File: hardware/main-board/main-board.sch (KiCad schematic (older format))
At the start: 0 parts

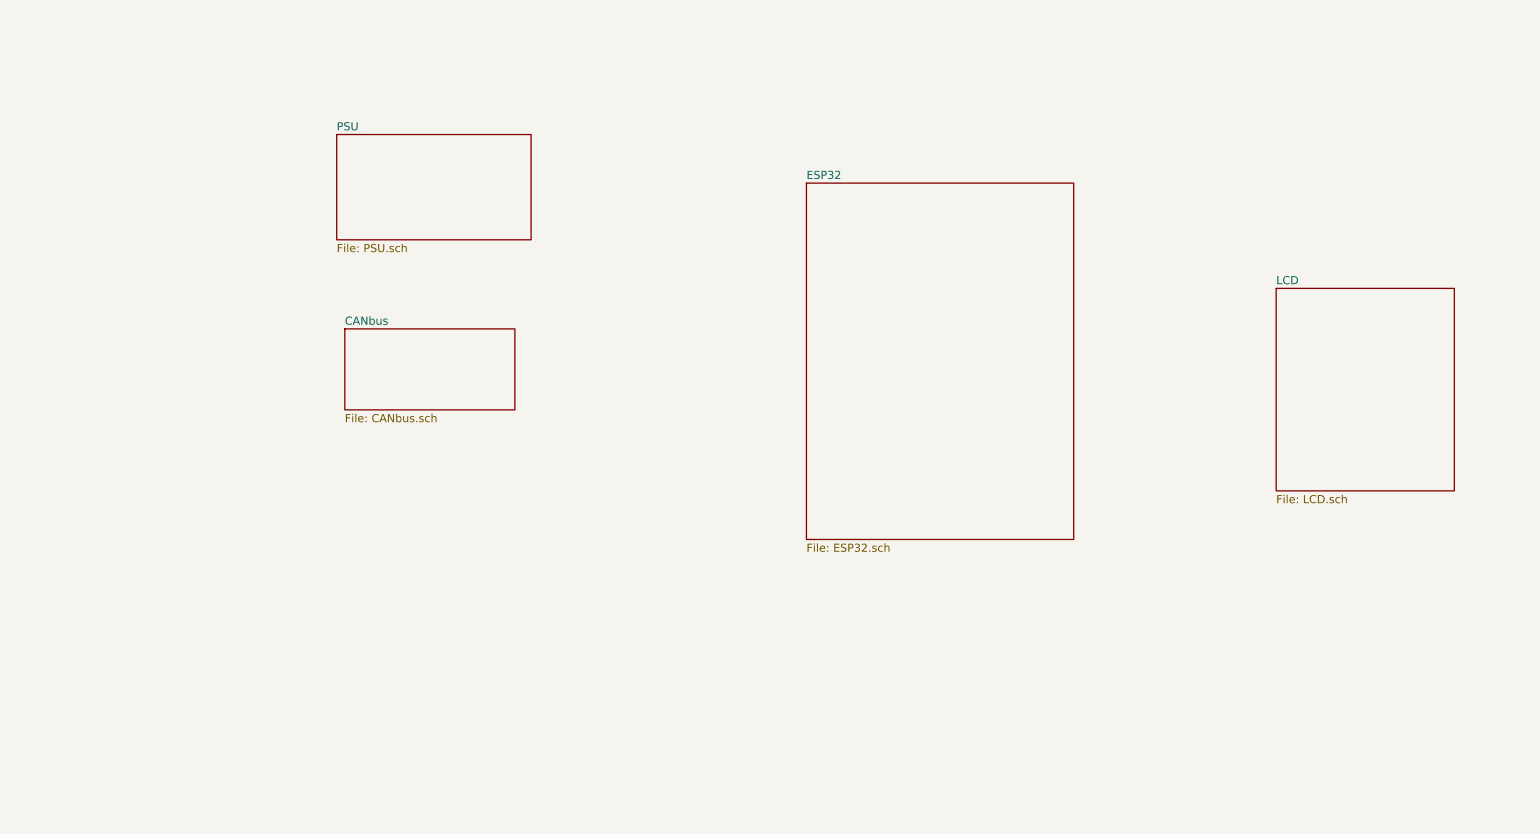
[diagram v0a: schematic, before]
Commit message: Sch mostly done, drew a few custom footprints, placement mostly done.
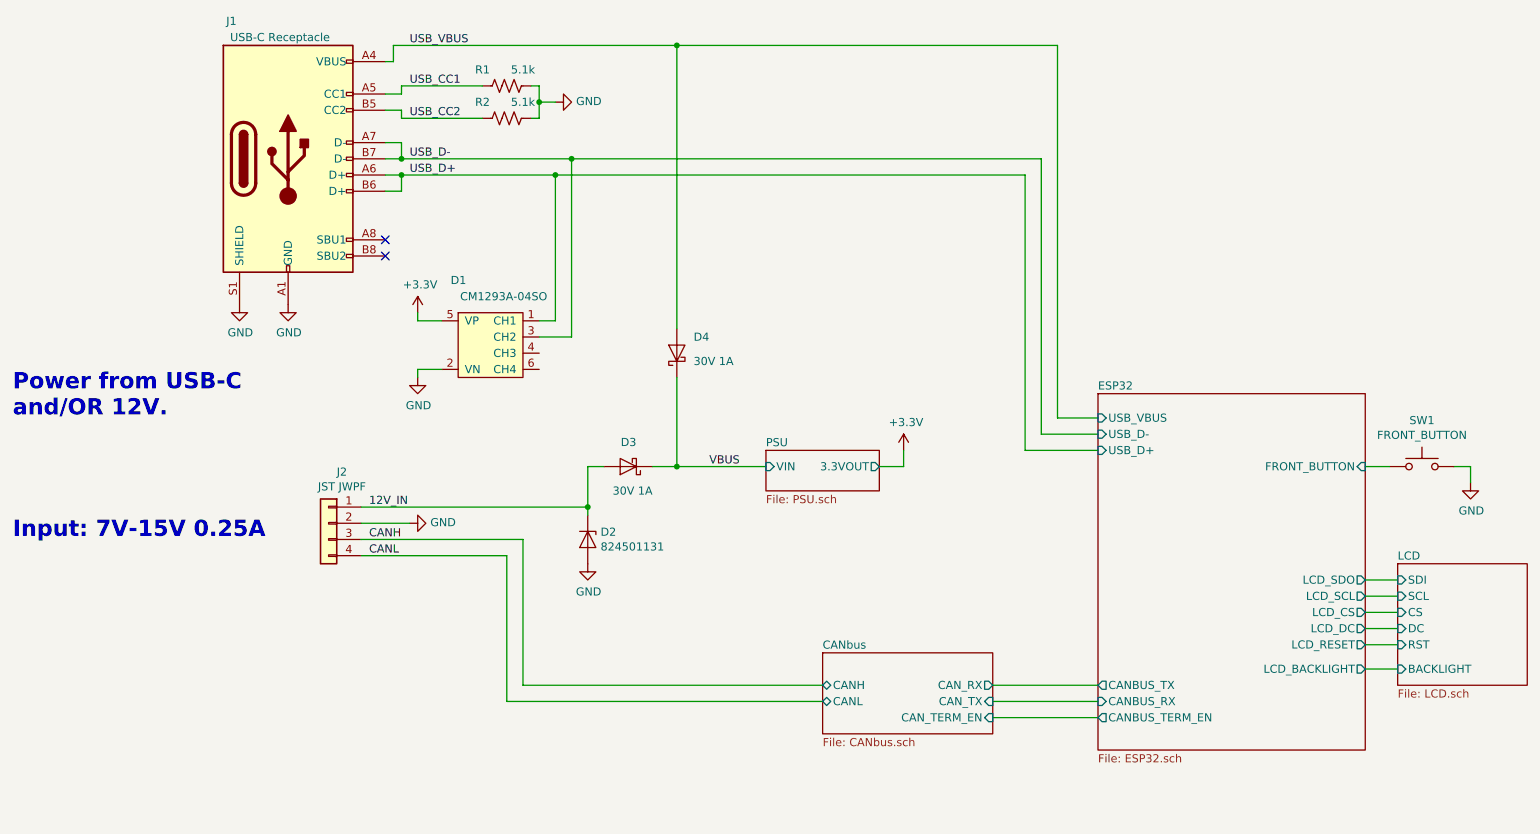
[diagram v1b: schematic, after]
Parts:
- added D1: CM1293A-04SO, Package_TO_SOT_SMD:SOT-23-6, symbol main-board-custom-symbols:CM1293A-04SO
- added D2: 824501131, Diode_SMD:D_SMA, symbol Device:D_Zener
- added D3, D4: 30V 1A, Diode_SMD:D_SMA, symbol Device:D_Schottky
- added J1: USB-C Receptacle, Connector_USB:USB_C_Receptacle_JAE_DX07S024WJ3R400, symbol Connector:USB_C_Receptacle_USB2.0
- added J2: JST JWPF, Connector_JST:JST_JWPF_B04B-JWPF-SK-R_1x04_P2.00mm_Vertical, symbol Connector_Generic:Conn_01x04
- added R1, R2: 5.1k, Resistor_SMD:R_0603_1608Metric, symbol Device:R_US
- added SW1: FRONT_BUTTON, Button_Switch_SMD:SW_SPST_B3S-1100, symbol Switch:SW_Push
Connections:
- new net +3V3: D1.5 (VP)
- new net 12V_IN: D2.1 (K), D3.2 (A), J2.1 (Pin_1)
- new net CANH: J2.3 (Pin_3)
- new net CANL: J2.4 (Pin_4)
- new net ESP32/FRONT_BUTTON: SW1.1
- new net GND: D1.2 (VN), D2.2 (A), J1.A1 (GND), J1.A12 (GND), J1.B1 (GND), J1.B12 (GND), J1.S1 (SHIELD), J2.2 (Pin_2), R1.1, R2.1, SW1.2
- new net USB_CC1: J1.A5 (CC1), R1.2
- new net USB_CC2: J1.B5 (CC2), R2.2
- new net USB_D+: D1.1 (CH1), J1.A6 (D+), J1.B6 (D+)
- new net USB_D-: D1.3 (CH2), J1.A7 (D-), J1.B7 (D-)
- new net USB_VBUS: D4.2 (A), J1.A4 (VBUS), J1.A9 (VBUS), J1.B4 (VBUS), J1.B9 (VBUS)
- new net VBUS: D3.1 (K), D4.1 (K)
- no-connect marks 0 -> 2
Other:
- note added: "Input: 7V-15V 0.25A"
- note added: "Power from USB-C\nand/OR 12V."

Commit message: layout almost done
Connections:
- net USB_D+: now also D1.3 (CH2); no longer D1.1 (CH1)
- net USB_D-: now also D1.1 (CH1); no longer D1.3 (CH2)
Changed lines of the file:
@@
 EESchema Schematic File Version 4
-LIBS:main-board-cache
-EELAYER 29 0
+EELAYER 30 0
 EELAYER END
 $Descr B 17000 11000
@@
 	5700 5950 5700 6850
 Wire Wire Line
-	6100 3500 9000 3500
-Wire Wire Line
-	5050 3500 6100 3500
-Connection ~ 6100 3500
-Wire Wire Line
-	6100 4600 6100 3500
-Wire Wire Line
-	6000 3600 8900 3600
-Wire Wire Line
-	5050 3600 6000 3600
-Connection ~ 6000 3600
-Wire Wire Line
-	6000 4500 6000 3600
-Wire Wire Line
 	5900 4600 6100 4600
 Wire Wire Line
 	5900 4500 6000 4500
+Wire Wire Line
+	5050 3500 6000 3500
+Wire Wire Line
+	5050 3600 6100 3600
+Wire Wire Line
+	6000 4500 6000 3500
+Connection ~ 6000 3500
+Wire Wire Line
+	6000 3500 9000 3500
+Wire Wire Line
+	6100 4600 6100 3600
+Connection ~ 6100 3600
+Wire Wire Line
+	6100 3600 8900 3600
 $EndSCHEMATC

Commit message: added all 3d
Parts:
- J1: footprint Connector_USB:USB_C_Receptacle_JAE_DX07S024WJ3R400 -> main-board-custom-footprints:USB_C_Receptacle_JAE_DX07S024WJ3R400
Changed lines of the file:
@@
 F 0 "J1" H 4000 4350 50  0000 C CNN
 F 1 "USB-C Receptacle" H 4300 4250 50  0000 C CNN
-F 2 "Connector_USB:USB_C_Receptacle_JAE_DX07S024WJ3R400" H 4500 3500 50  0001 C CNN
+F 2 "main-board-custom-footprints:USB_C_Receptacle_JAE_DX07S024WJ3R400" H 4500 3500 50  0001 C CNN
 F 3 "https://www.usb.org/sites/default/files/documents/usb_type-c.zip" H 4500 3500 50  0001 C CNN
 F 4 "DX07S024WJ3R400" H 4350 3500 50  0001 C CNN "MPN"

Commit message: SO-8 3d added, layout done
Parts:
- J2: footprint Connector_JST:JST_JWPF_B04B-JWPF-SK-R_1x04_P2.00mm_Vertical -> main-board-custom-footprints:JST_JWPF_B04B-JWPF-SK-R_1x04_P2.00mm_Vertical
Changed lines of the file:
@@
 F 0 "J2" H 4518 6067 50  0000 C CNN
 F 1 "JST JWPF" H 4518 5976 50  0000 C CNN
-F 2 "Connector_JST:JST_JWPF_B04B-JWPF-SK-R_1x04_P2.00mm_Vertical" H 4600 5750 50  0001 C CNN
+F 2 "main-board-custom-footprints:JST_JWPF_B04B-JWPF-SK-R_1x04_P2.00mm_Vertical" H 4600 5750 50  0001 C CNN
 F 3 "~" H 4600 5750 50  0001 C CNN
 F 4 "B04B-JWPF-SK-R(LF)(SN)" H 4600 5750 50  0001 C CNN "MPN"

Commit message: updated LCD to proper board footprint, added additional 3d models
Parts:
- SW1: footprint Button_Switch_SMD:SW_SPST_B3S-1100 -> main-board-custom-footprints:SW_SPST_B3S-1100
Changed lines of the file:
@@
 EESchema Schematic File Version 4
-EELAYER 30 0
+LIBS:main-board-cache
+EELAYER 29 0
 EELAYER END
 $Descr B 17000 11000
@@
 F 0 "SW1" H 11350 5685 50  0000 C CNN
 F 1 "FRONT_BUTTON" H 11350 5594 50  0000 C CNN
-F 2 "Button_Switch_SMD:SW_SPST_B3S-1100" H 11350 5600 50  0001 C CNN
+F 2 "main-board-custom-footprints:SW_SPST_B3S-1100" H 11350 5600 50  0001 C CNN
 F 3 "~" H 11350 5600 50  0001 C CNN
 F 4 "B3S-1100P" H 11350 5400 50  0001 C CNN "MPN"

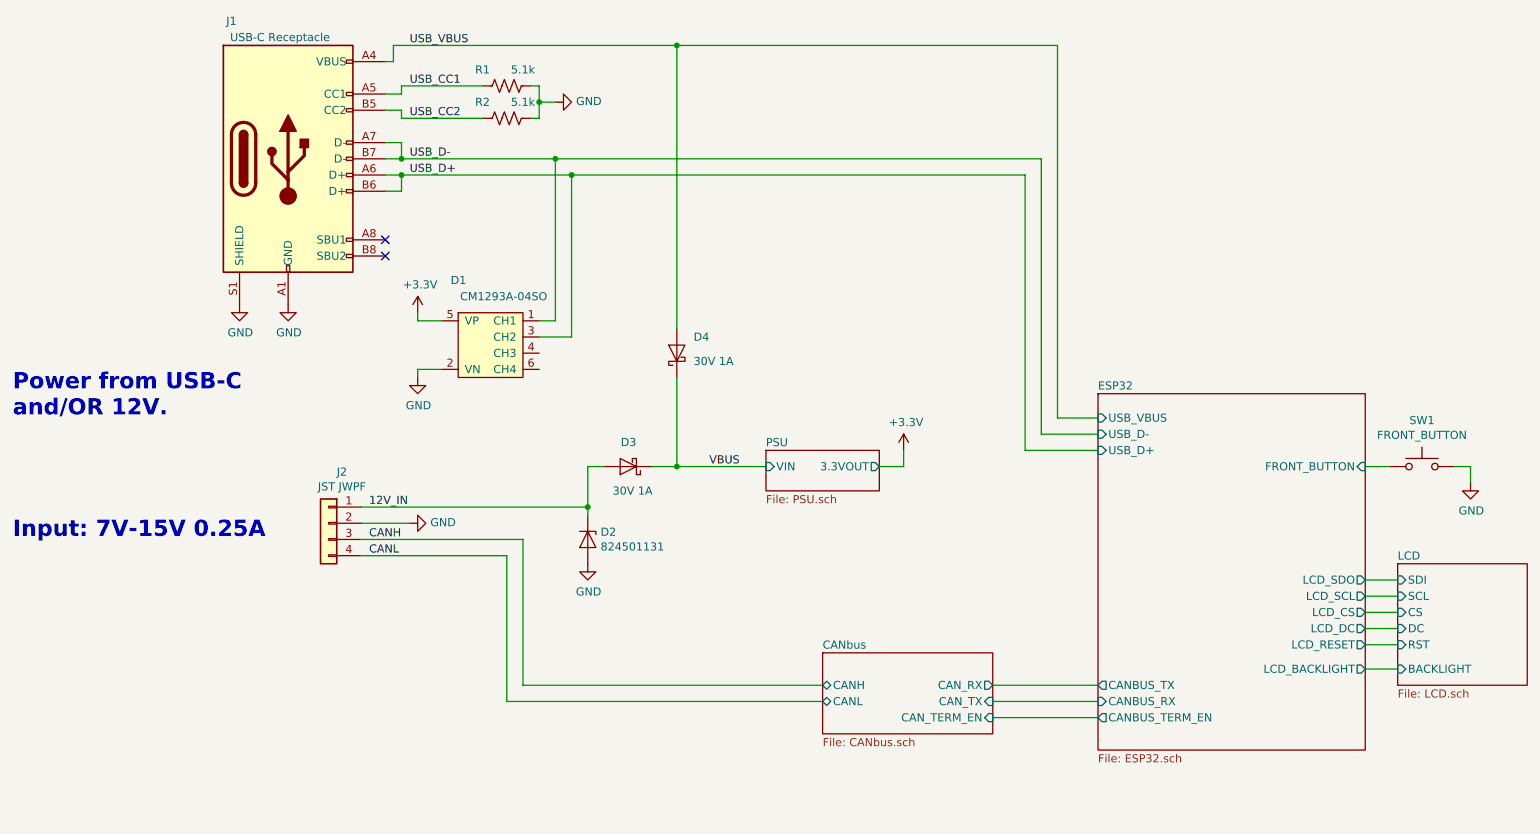
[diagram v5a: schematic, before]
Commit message: added qr code, switched button to a different button. put on reddit for review
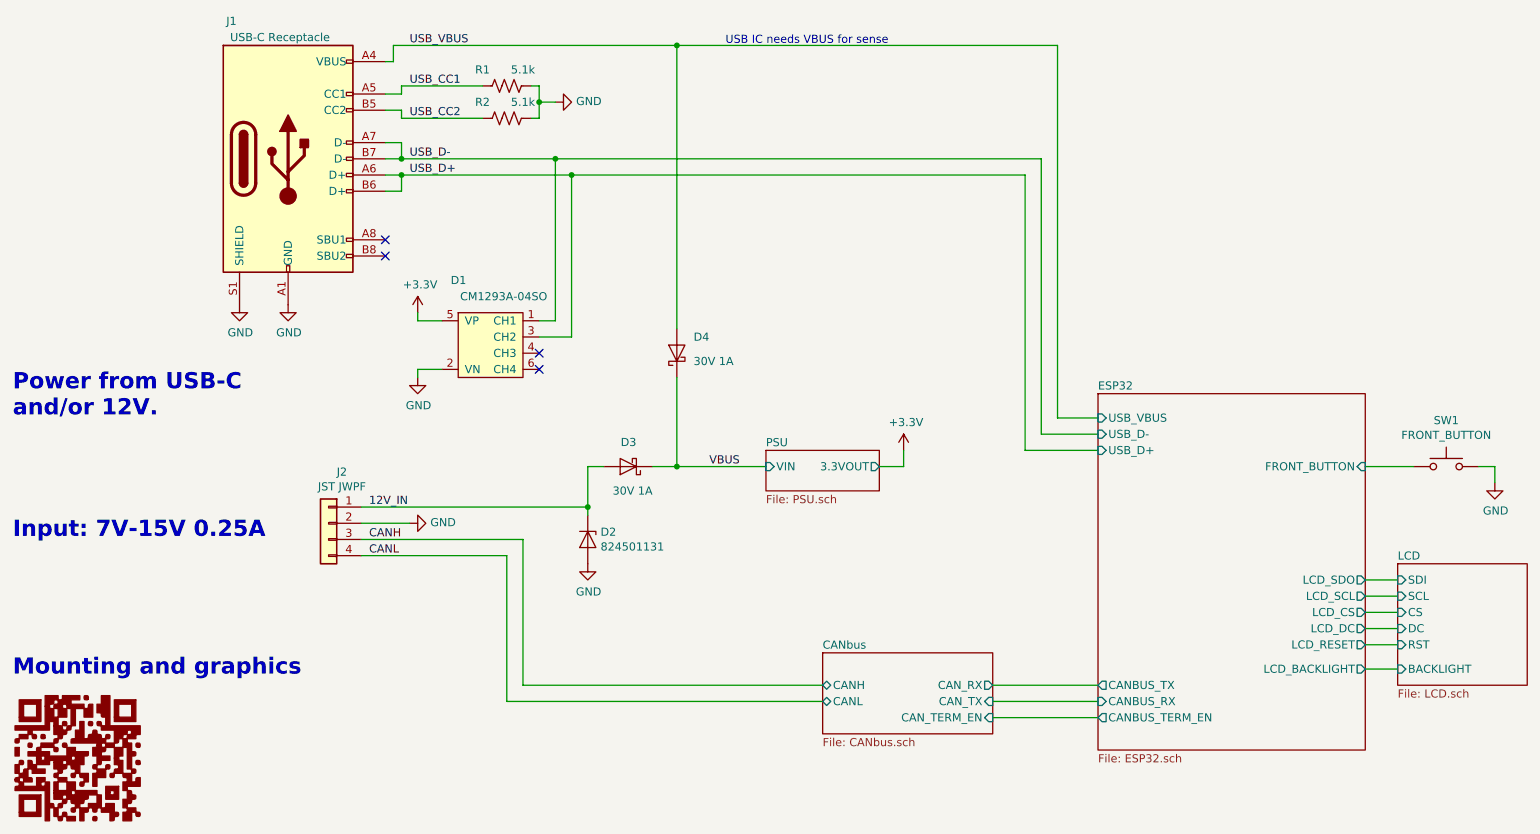
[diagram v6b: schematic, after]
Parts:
- added G1: LOGO, main-board-custom-footprints:gcan-gauge-github-link-qr, symbol gcan-gauge-github-link-qr:LOGO
- SW1: footprint main-board-custom-footprints:SW_SPST_B3S-1100 -> main-board-custom-footprints:SW_SPST_PTS810
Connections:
- no-connect marks 2 -> 4
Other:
- note added: "Mounting and graphics"
- note added: "Power from USB-C\nand/or 12V."
- note added: "USB IC needs VBUS for sense"
- note removed: "Power from USB-C\nand/OR 12V."
- moved on the sheet: SW1
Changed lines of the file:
@@
 EESchema Schematic File Version 4
-LIBS:main-board-cache
-EELAYER 29 0
+EELAYER 30 0
 EELAYER END
 $Descr B 17000 11000
@@
 L Switch:SW_Push SW1
 U 1 1 60FA2104
-P 11350 5400
-F 0 "SW1" H 11350 5685 50  0000 C CNN
-F 1 "FRONT_BUTTON" H 11350 5594 50  0000 C CNN
-F 2 "main-board-custom-footprints:SW_SPST_B3S-1100" H 11350 5600 50  0001 C CNN
-F 3 "~" H 11350 5600 50  0001 C CNN
-F 4 "B3S-1100P" H 11350 5400 50  0001 C CNN "MPN"
-	1    11350 5400
-	1    0    0    -1
-$EndComp
-Wire Wire Line
-	11000 5400 11150 5400
+P 11500 5400
+F 0 "SW1" H 11500 5685 50  0000 C CNN
+F 1 "FRONT_BUTTON" H 11500 5594 50  0000 C CNN
+F 2 "main-board-custom-footprints:SW_SPST_PTS810" H 11500 5600 50  0001 C CNN
+F 3 "~" H 11500 5600 50  0001 C CNN
+F 4 "B3S-1100P" H 11500 5400 50  0001 C CNN "MPN"
+	1    11500 5400
+	1    0    0    -1
+$EndComp
+Wire Wire Line
+	11000 5400 11300 5400
 $Comp
 L power:GND #PWR09
 U 1 1 60FAD266
-P 11650 5500
-F 0 "#PWR09" H 11650 5250 50  0001 C CNN
-F 1 "GND" H 11655 5327 50  0000 C CNN
-F 2 "" H 11650 5500 50  0001 C CNN
-F 3 "" H 11650 5500 50  0001 C CNN
-	1    11650 5500
-	1    0    0    -1
-$EndComp
-Wire Wire Line
-	11550 5400 11650 5400
-Wire Wire Line
-	11650 5400 11650 5500
+P 11800 5500
+F 0 "#PWR09" H 11800 5250 50  0001 C CNN
+F 1 "GND" H 11805 5327 50  0000 C CNN
+F 2 "" H 11800 5500 50  0001 C CNN
+F 3 "" H 11800 5500 50  0001 C CNN
+	1    11800 5500
+	1    0    0    -1
+$EndComp
+Wire Wire Line
+	11700 5400 11800 5400
+Wire Wire Line
+	11800 5400 11800 5500
 Wire Wire Line
 	11000 6100 11200 6100
@@
 Input: 7V-15V 0.25A
 Text Notes 2650 5100 0    100  ~ 20
-Power from USB-C\nand/OR 12V.
+Power from USB-C\nand/or 12V.
 Wire Wire Line
 	5800 5850 5800 6750
@@
 Wire Wire Line
 	6100 3600 8900 3600
+NoConn ~ 5900 4700
+NoConn ~ 5900 4800
+Text Notes 2650 6700 0    100  ~ 20
+Mounting and graphics
+$Comp
+L gcan-gauge-github-link-qr:LOGO G1
+U 1 1 61095E2F
+P 3050 7200
+F 0 "G1" H 3050 6844 60  0001 C CNN
+F 1 "LOGO" H 3050 7556 60  0001 C CNN
+F 2 "main-board-custom-footprints:gcan-gauge-github-link-qr" H 3050 7200 50  0001 C CNN
+F 3 "" H 3050 7200 50  0001 C CNN
+	1    3050 7200
+	1    0    0    -1
+$EndComp
+Text Notes 7050 2800 0    50   ~ 0
+USB IC needs VBUS for sense
 $EndSCHEMATC

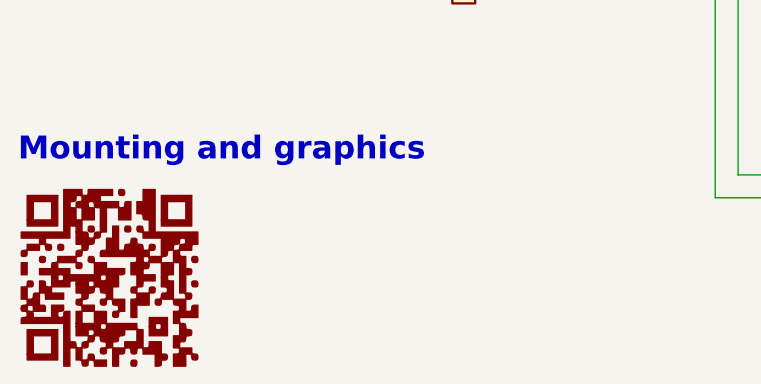
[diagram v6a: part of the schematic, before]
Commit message: Added mounting holes, tweaked layout to accomodate.
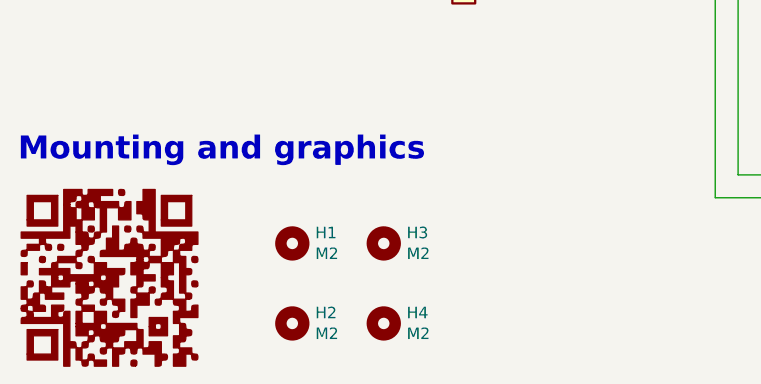
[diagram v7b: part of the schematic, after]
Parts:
- added H1, H2, H3, H4: M2, MountingHole:MountingHole_2.1mm, symbol Mechanical:MountingHole
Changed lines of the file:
@@
 EESchema Schematic File Version 4
-EELAYER 30 0
+LIBS:main-board-cache
+EELAYER 29 0
 EELAYER END
 $Descr B 17000 11000
@@
 Text Notes 7050 2800 0    50   ~ 0
 USB IC needs VBUS for sense
+$Comp
+L Mechanical:MountingHole H1
+U 1 1 610C9B41
+P 3850 7050
+F 0 "H1" H 3950 7096 50  0000 L CNN
+F 1 "M2" H 3950 7005 50  0000 L CNN
+F 2 "MountingHole:MountingHole_2.1mm" H 3850 7050 50  0001 C CNN
+F 3 "~" H 3850 7050 50  0001 C CNN
+	1    3850 7050
+	1    0    0    -1
+$EndComp
+$Comp
+L Mechanical:MountingHole H3
+U 1 1 610CA4FC
+P 4250 7050
+F 0 "H3" H 4350 7096 50  0000 L CNN
+F 1 "M2" H 4350 7005 50  0000 L CNN
+F 2 "MountingHole:MountingHole_2.1mm" H 4250 7050 50  0001 C CNN
+F 3 "~" H 4250 7050 50  0001 C CNN
+	1    4250 7050
+	1    0    0    -1
+$EndComp
+$Comp
+L Mechanical:MountingHole H2
+U 1 1 610CA73F
+P 3850 7400
+F 0 "H2" H 3950 7446 50  0000 L CNN
+F 1 "M2" H 3950 7355 50  0000 L CNN
+F 2 "MountingHole:MountingHole_2.1mm" H 3850 7400 50  0001 C CNN
+F 3 "~" H 3850 7400 50  0001 C CNN
+	1    3850 7400
+	1    0    0    -1
+$EndComp
+$Comp
+L Mechanical:MountingHole H4
+U 1 1 610CA9AE
+P 4250 7400
+F 0 "H4" H 4350 7446 50  0000 L CNN
+F 1 "M2" H 4350 7355 50  0000 L CNN
+F 2 "MountingHole:MountingHole_2.1mm" H 4250 7400 50  0001 C CNN
+F 3 "~" H 4250 7400 50  0001 C CNN
+	1    4250 7400
+	1    0    0    -1
+$EndComp
 $EndSCHEMATC

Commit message: BOM cleanup/adding MPNs
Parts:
- G1, H1, H2, H3, H4: MPN (none) -> DNP
- R1, R2: MPN (none) -> RC0603JR-075K1L
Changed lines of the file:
@@
 F 2 "Resistor_SMD:R_0603_1608Metric" V 5740 3040 50  0001 C CNN
 F 3 "~" H 5700 3050 50  0001 C CNN
+F 4 "RC0603JR-075K1L" H 5700 3050 50  0001 C CNN "MPN"
 	1    5700 3050
 	0    1    1    0
@@
 F 2 "Resistor_SMD:R_0603_1608Metric" V 5740 3240 50  0001 C CNN
 F 3 "~" H 5700 3250 50  0001 C CNN
+F 4 "RC0603JR-075K1L" H 5700 3250 50  0001 C CNN "MPN"
 	1    5700 3250
 	0    1    1    0
@@
 F 2 "main-board-custom-footprints:gcan-gauge-github-link-qr" H 3050 7200 50  0001 C CNN
 F 3 "" H 3050 7200 50  0001 C CNN
+F 4 "DNP" H 3050 7200 50  0001 C CNN "MPN"
 	1    3050 7200
 	1    0    0    -1
@@
 F 2 "MountingHole:MountingHole_2.1mm" H 3850 7050 50  0001 C CNN
 F 3 "~" H 3850 7050 50  0001 C CNN
+F 4 "DNP" H 3850 7050 50  0001 C CNN "MPN"
 	1    3850 7050
 	1    0    0    -1
@@
 F 2 "MountingHole:MountingHole_2.1mm" H 4250 7050 50  0001 C CNN
 F 3 "~" H 4250 7050 50  0001 C CNN
+F 4 "DNP" H 4250 7050 50  0001 C CNN "MPN"
 	1    4250 7050
 	1    0    0    -1
@@
 F 2 "MountingHole:MountingHole_2.1mm" H 3850 7400 50  0001 C CNN
 F 3 "~" H 3850 7400 50  0001 C CNN
+F 4 "DNP" H 3850 7400 50  0001 C CNN "MPN"
 	1    3850 7400
 	1    0    0    -1
@@
 F 2 "MountingHole:MountingHole_2.1mm" H 4250 7400 50  0001 C CNN
 F 3 "~" H 4250 7400 50  0001 C CNN
+F 4 "DNP" H 4250 7400 50  0001 C CNN "MPN"
 	1    4250 7400
 	1    0    0    -1
